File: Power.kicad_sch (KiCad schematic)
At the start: 39 parts, among them J7 Barrel_Jack, J8 Conn_01x02, U3 TLV75533PDRV, U6 LMR51450FNDRR, U7 LMR51450FNDRR, U8 TPS259472LRPWR

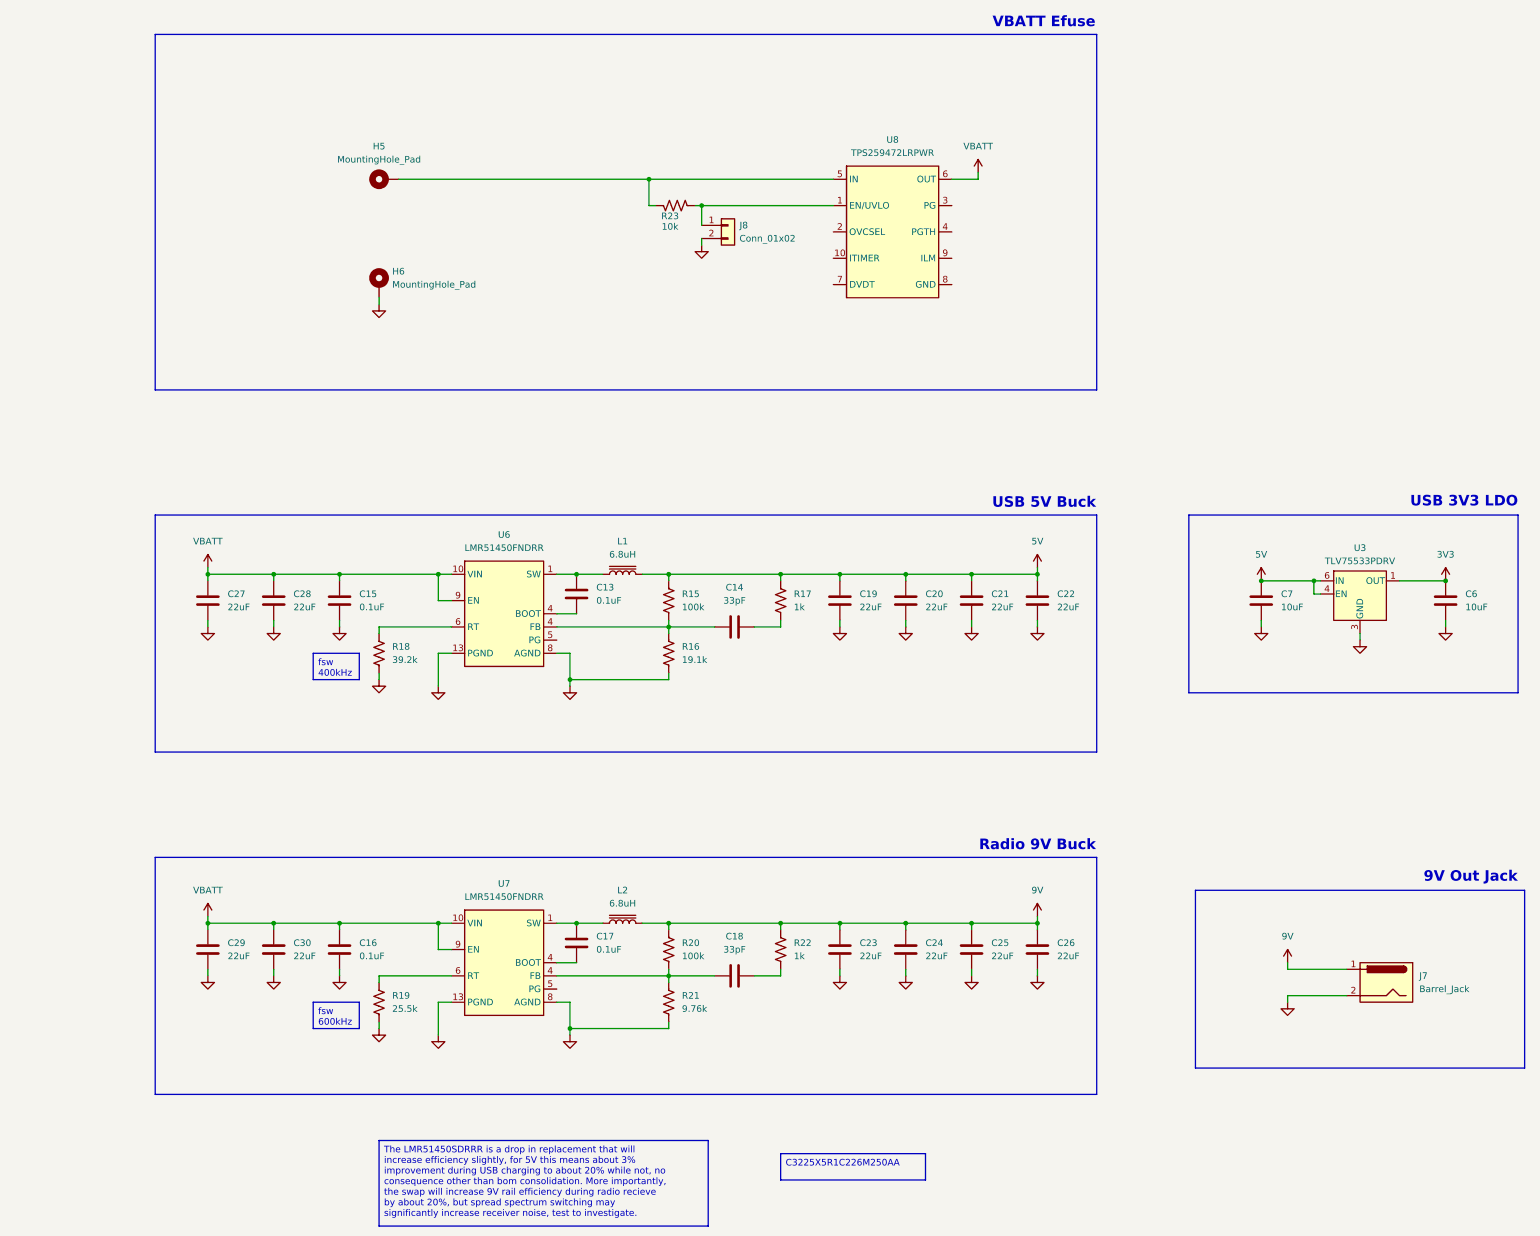
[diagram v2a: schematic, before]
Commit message: finish efuse schematic, update connectors
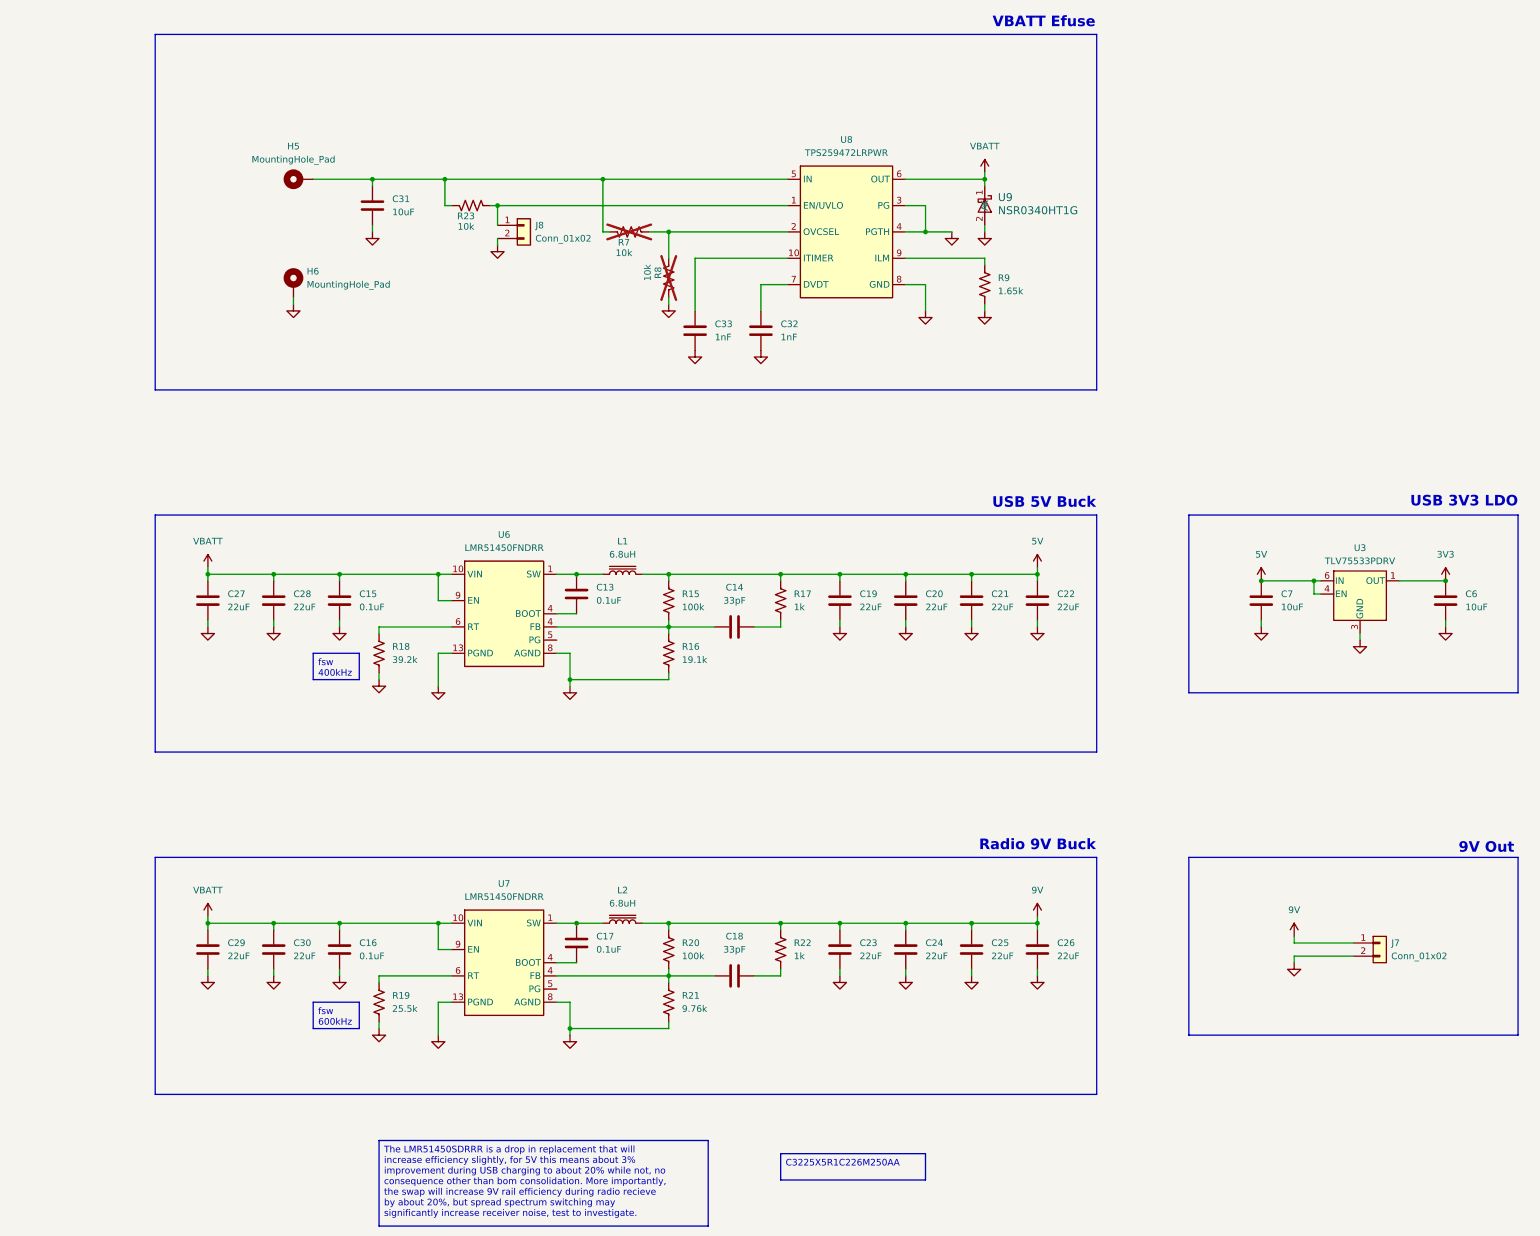
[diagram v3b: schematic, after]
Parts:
- removed J7: Barrel_Jack, Cave_Radio_PDB:CUI_PJ-102A, symbol Cave_Radio_PDB:Barrel_Jack
- added C31: 10uF, Cave_Radio_PDB:C_0402_1005Metric, symbol Cave_Radio_PDB:10uF
- added C32, C33: 1nF, symbol Cave_Radio_PDB:1nF
- added J7: Conn_01x02, Cave_Radio_PDB:CONN_TSW-102-S_SAI, symbol Cave_Radio_PDB:Conn_01x02
- added R7, R8: 10k, Cave_Radio_PDB:R_0402_1005Metric, symbol Cave_Radio_PDB:10k
- added R9: 1.65k, symbol Cave_Radio_PDB:1.65k
- added U9: NSR0340HT1G, SOD-323_1P8X1P35_ONS, symbol Cave_Radio_PDB:NSR0340HT1G
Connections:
- net 9V: now also J7.1 (Pin_1)
- net GND: now also U8.3 (PG), U8.4 (PGTH), U8.8 (GND), C31.2, C32.2, C33.2, J7.2 (Pin_2), R8.2, R9.2, U9.2 (A)
- net VBATT: now also U9.1 (K)
- net at H5.1, R23.1, U8.5 (IN): now also C31.1, R7.1
- net at U8.10 (ITIMER): now also C33.1
- net at U8.2 (OVCSEL): now also R7.2, R8.1
- net at U8.7 (DVDT): now also C32.1
- net at U8.9 (ILM): now also R9.1
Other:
- note added: "9V Out"
- note removed: "9V Out Jack"
- moved on the sheet: H5, H6, J8, R23, U8

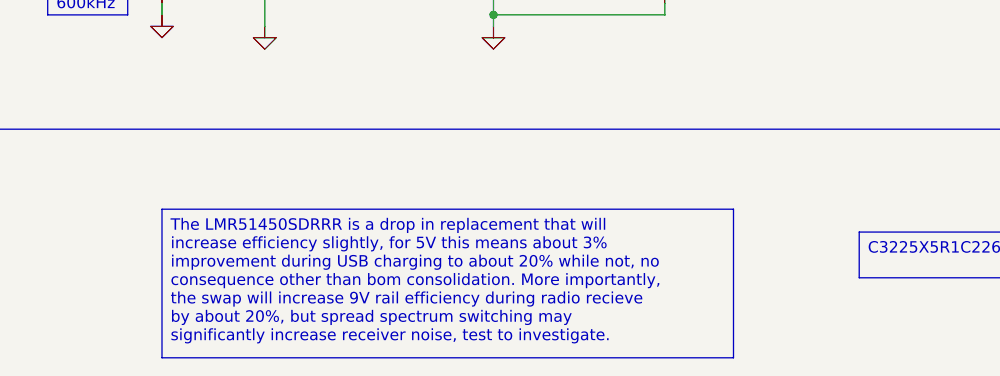
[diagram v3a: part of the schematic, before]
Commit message: Update footprints
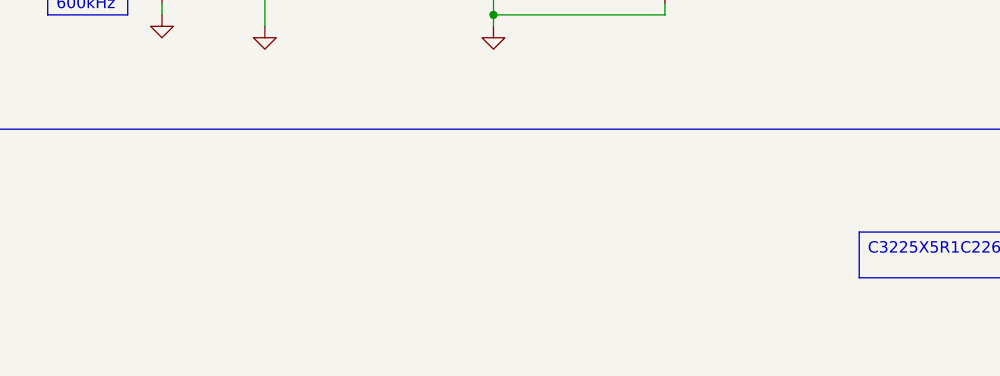
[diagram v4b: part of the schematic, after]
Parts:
- C31, C6, C7: footprint Cave_Radio_PDB:C_0402_1005Metric -> Cave_Radio_PDB:R_0603_1608Metric
- C32, C33: footprint (none) -> Cave_Radio_PDB:C_0402_1005Metric
- R9: footprint (none) -> Cave_Radio_PDB:R_0402_1005Metric
- U3: footprint Package_SON:WSON-6-1EP_2x2mm_P0.65mm_EP1x1.6mm -> Cave_Radio_PDB:WSON-6-1EP_2x2mm_P0.65mm_EP1x1.6mm_ThermalVias
- U8: footprint Package_SON:VSON-10-1EP_3x3mm_P0.5mm_EP1.65x2.4mm_ThermalVias -> Cave_Radio_PDB:VSON-10-1EP_3x3mm_P0.5mm_EP1.65x2.4mm_ThermalVias
- U9: footprint SOD-323_1P8X1P35_ONS -> Cave_Radio_PDB:SOD-323_1P8X1P35_ONS
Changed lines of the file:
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@@
 		)
 	)
-	(text_box "The LMR51450SDRRR is a drop in replacement that will increase efficiency slightly, for 5V this means about 3% improvement during USB charging to about 20% while not, no consequence other than bom consolidation. More importantly, the swap will increase 9V rail efficiency during radio recieve by about 20%, but spread spectrum switching may significantly increase receiver noise, test to investigate."
-		(exclude_from_sim no)
-		(at 143.51 251.46 0)
-		(size 63.5 16.51)
-		(margins 0.9525 0.9525 0.9525 0.9525)
-		(stroke
-			(width 0)
-			(type solid)
-		)
-		(fill
-			(type none)
-		)
-		(effects
-			(font
-				(size 1.27 1.27)
-			)
-			(justify left top)
-		)
-	)
 	(text_box "C3225X5R1C226M250AA"
 		(exclude_from_sim no)
@@
 			)
 		)
-		(property "Footprint" ""
+		(property "Footprint" "Cave_Radio_PDB:R_0402_1005Metric"
 			(at 261.366 86.614 90)
 			(effects
@@
 			)
 		)
-		(property "Footprint" ""
+		(property "Footprint" "Cave_Radio_PDB:C_0402_1005Metric"
 			(at 218.1352 99.06 0)
 			(effects
@@
 			)
 		)
-		(property "Footprint" ""
+		(property "Footprint" "Cave_Radio_PDB:C_0402_1005Metric"
 			(at 205.4352 99.06 0)
 			(effects
@@
 			)
 		)
-		(property "Footprint" "Package_SON:VSON-10-1EP_3x3mm_P0.5mm_EP1.65x2.4mm_ThermalVias"
+		(property "Footprint" "Cave_Radio_PDB:VSON-10-1EP_3x3mm_P0.5mm_EP1.65x2.4mm_ThermalVias"
 			(at 232.41 96.52 0)
 			(effects
@@
 			)
 		)
-		(property "Footprint" "Cave_Radio_PDB:C_0402_1005Metric"
+		(property "Footprint" "Cave_Radio_PDB:R_0603_1608Metric"
 			(at 350.2152 151.13 0)
 			(effects
@@
 			)
 		)
-		(property "Footprint" "SOD-323_1P8X1P35_ONS"
+		(property "Footprint" "Cave_Radio_PDB:SOD-323_1P8X1P35_ONS"
 			(at 277.876 79.756 0)
 			(effects
@@
 			)
 		)
-		(property "Footprint" "Cave_Radio_PDB:C_0402_1005Metric"
+		(property "Footprint" "Cave_Radio_PDB:R_0603_1608Metric"
 			(at 314.6552 151.13 0)
 			(effects
@@
 			)
 		)
-		(property "Footprint" "Package_SON:WSON-6-1EP_2x2mm_P0.65mm_EP1x1.6mm"
+		(property "Footprint" "Cave_Radio_PDB:WSON-6-1EP_2x2mm_P0.65mm_EP1x1.6mm_ThermalVias"
 			(at 332.74 137.795 0)
 			(effects
@@
 			)
 		)
-		(property "Footprint" "Cave_Radio_PDB:C_0402_1005Metric"
+		(property "Footprint" "Cave_Radio_PDB:R_0603_1608Metric"
 			(at 143.2052 74.93 0)
 			(effects

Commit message: start layout
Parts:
- removed H5, H6: MountingHole_Pad, Cave_Radio_PDB:MountingHole_3.2mm_M3_DIN965_Pad_TopBottom, symbol Cave_Radio_PDB:MountingHole_Pad
- added J1: Conn_01x02, Cave_Radio_PDB:CONN_102_PWR, symbol Cave_Radio_PDB:Conn_01x02
- U8: footprint Cave_Radio_PDB:VSON-10-1EP_3x3mm_P0.5mm_EP1.65x2.4mm_ThermalVias -> Cave_Radio_PDB:VQFN8_PWR_TEX
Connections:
- net 9V: now also J7.2 (Pin_2); no longer J7.1 (Pin_1)
- net GND: now also J7.1 (Pin_1), R23.1, J1.1 (Pin_1); no longer J7.2 (Pin_2), J8.2 (Pin_2)
- net at C14.1, R15.2, R16.1: now also U6.7 (FB); no longer U6.4 (FB)
- net at C31.1, R7.1, U8.5 (IN): now also J8.1 (Pin_1), J1.2 (Pin_2); no longer R23.1
- net at R23.2, U8.1 (EN/UVLO): now also J8.2 (Pin_2); no longer J8.1 (Pin_1)
- net at C18.1, R20.2, R21.1: now also U7.7 (FB); no longer U7.4 (FB)
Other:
- moved on the sheet: J8, R23
